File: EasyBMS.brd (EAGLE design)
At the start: 49 x 100 mm, 166 parts, among them IC1 LM2596S-5.0_NOPB, IC2 LTC6811IG-1#PBF, Q10 BSS84LT1G, Q11 BSS84LT1G, Q12 BSS84LT1G, Q13 BSS84LT1G, Q2 BSS84LT1G, Q3 BSS84LT1G, Q4 BSS84LT1G, Q5 BSS84LT1G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

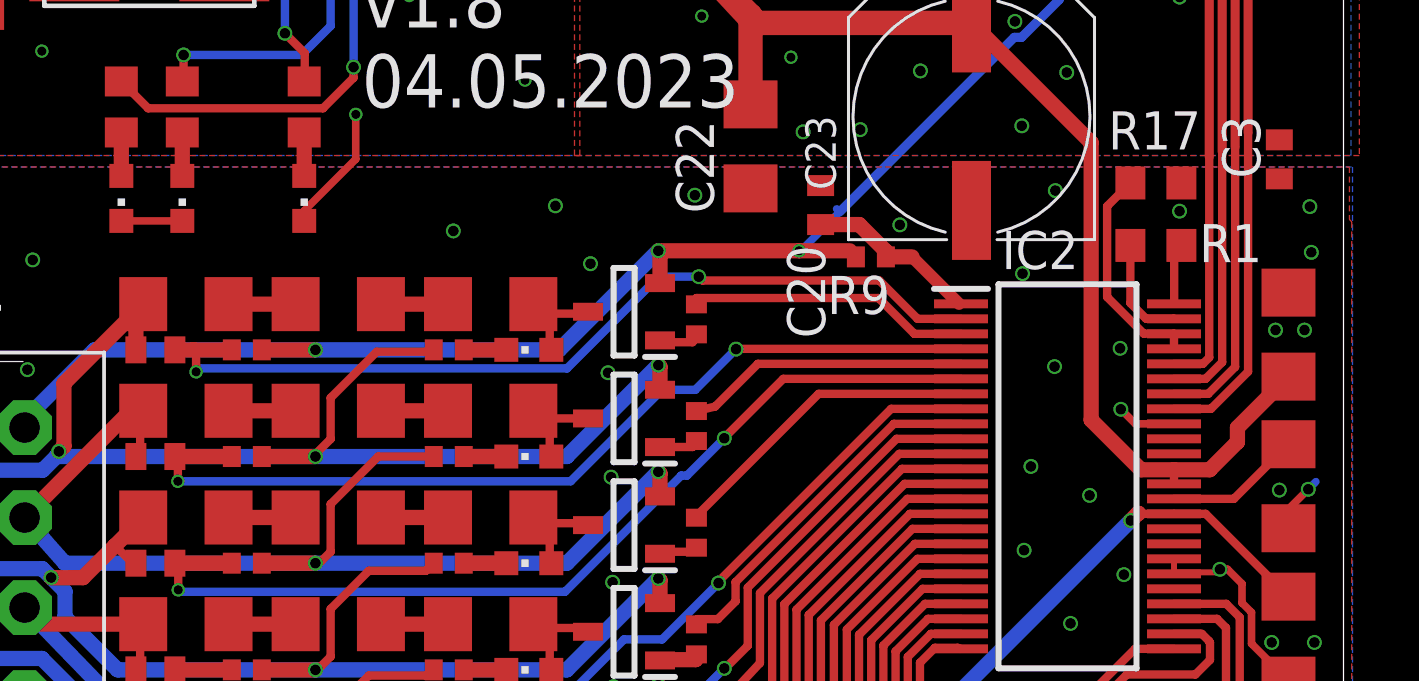
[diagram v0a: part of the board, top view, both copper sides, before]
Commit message: bug on 2 LEDs removed, new production files generated
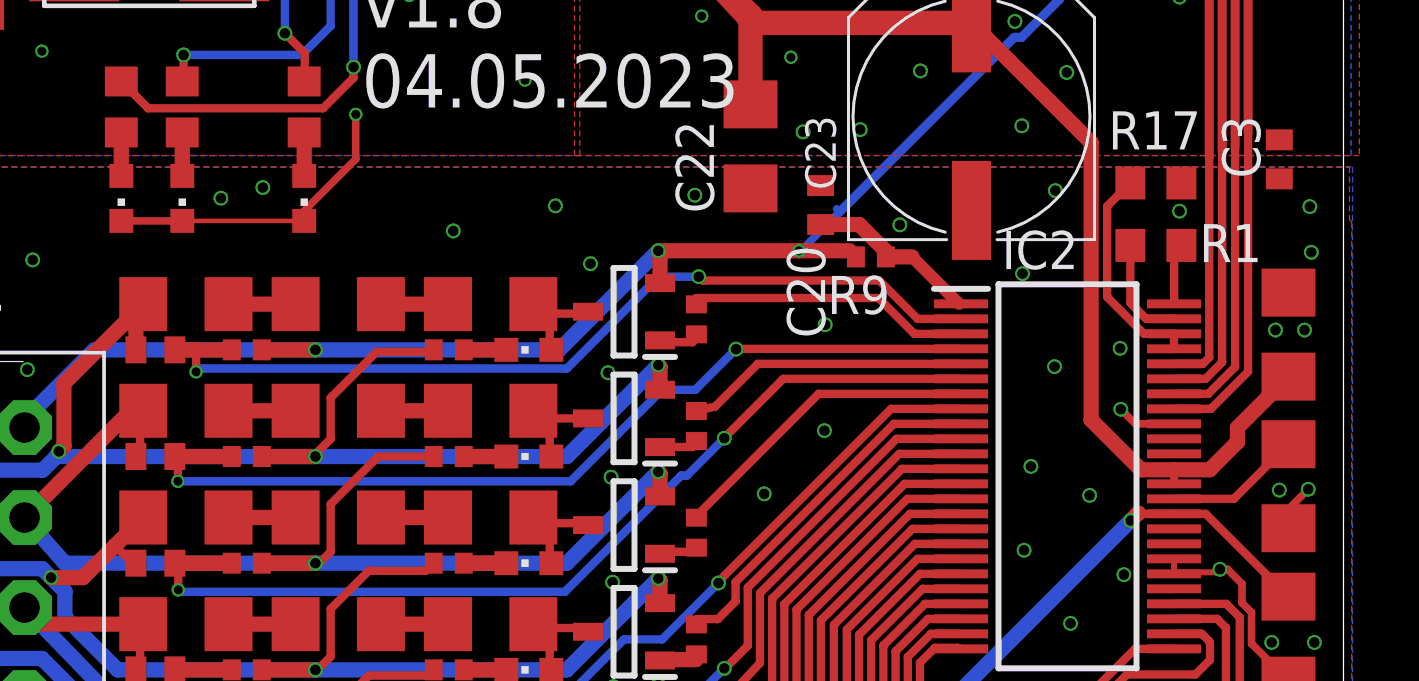
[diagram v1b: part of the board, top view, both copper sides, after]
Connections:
- removed net N$3: LED1.C, LED2.C
- net GND: now also LED1.C, LED2.C
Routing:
- net GND: track 40.3 -> 46.4 mm
- net N$3: track 2.03 -> 0.00 mm
- net GND2: track 10.9 -> 10.5 mm, vias 70 -> 75
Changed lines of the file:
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@@
 <via x="44.958" y="79.74" extent="1-16" drill="0.3"/>
 <via x="44.8056" y="76.6158" extent="1-16" drill="0.3"/>
+<contactref element="LED2" pad="C"/>
+<contactref element="LED1" pad="C"/>
+<wire x1="10.2944" y1="50.2718" x2="8.2624" y2="50.2718" width="0.254" layer="1"/>
+<wire x1="10.2944" y1="50.2718" x2="14.3584" y2="50.2718" width="0.1524" layer="1"/>
 </signal>
 <signal name="N$202">
@@
 <wire x1="47.1678" y1="40.6654" x2="47.8282" y2="41.3258" width="0.254" layer="1"/>
 <via x="47.8282" y="41.3258" extent="1-16" drill="0.35"/>
-<wire x1="47.8282" y1="41.3258" x2="48.0822" y2="41.5798" width="0.254" layer="16"/>
 <via x="47.7012" y="46.6344" extent="1-16" drill="0.35"/>
 <via x="46.863" y="41.3004" extent="1-16" drill="0.35"/>
@@
 <via x="38.3032" y="48.514" extent="1-16" drill="0.35"/>
 <via x="38.5826" y="42.0878" extent="1-16" drill="0.35"/>
-</signal>
-<signal name="N$3">
-<contactref element="LED2" pad="C"/>
-<contactref element="LED1" pad="C"/>
-<wire x1="10.2944" y1="50.2718" x2="8.2624" y2="50.2718" width="0.254" layer="1"/>
+<via x="12.9794" y="51.3842" extent="1-16" drill="0.35"/>
+<via x="11.5824" y="51.0286" extent="1-16" drill="0.35"/>
+<via x="31.6992" y="43.2816" extent="1-16" drill="0.35"/>
+<via x="29.6926" y="41.1734" extent="1-16" drill="0.35"/>
+<via x="31.7246" y="46.8122" extent="1-16" drill="0.35"/>
 </signal>
 <signal name="A0DC">

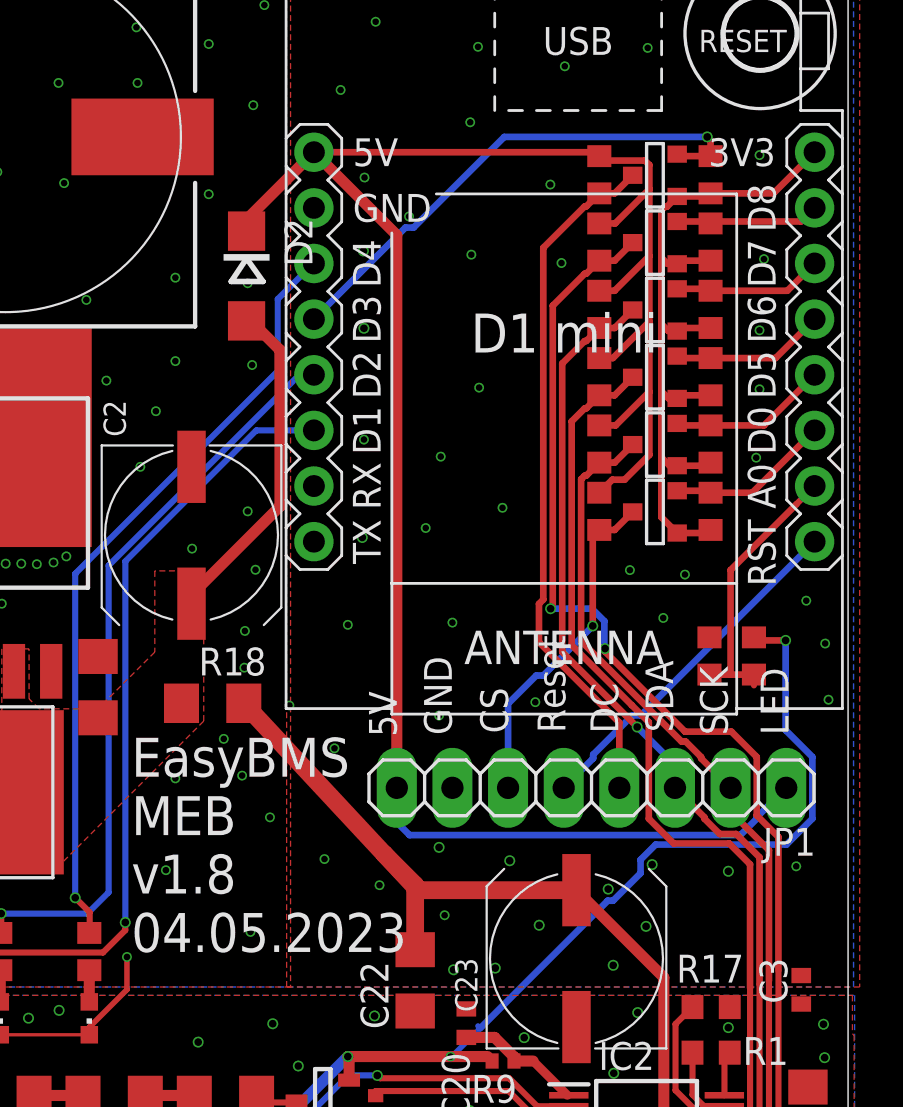
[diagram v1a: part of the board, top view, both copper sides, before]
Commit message: level shifter removed
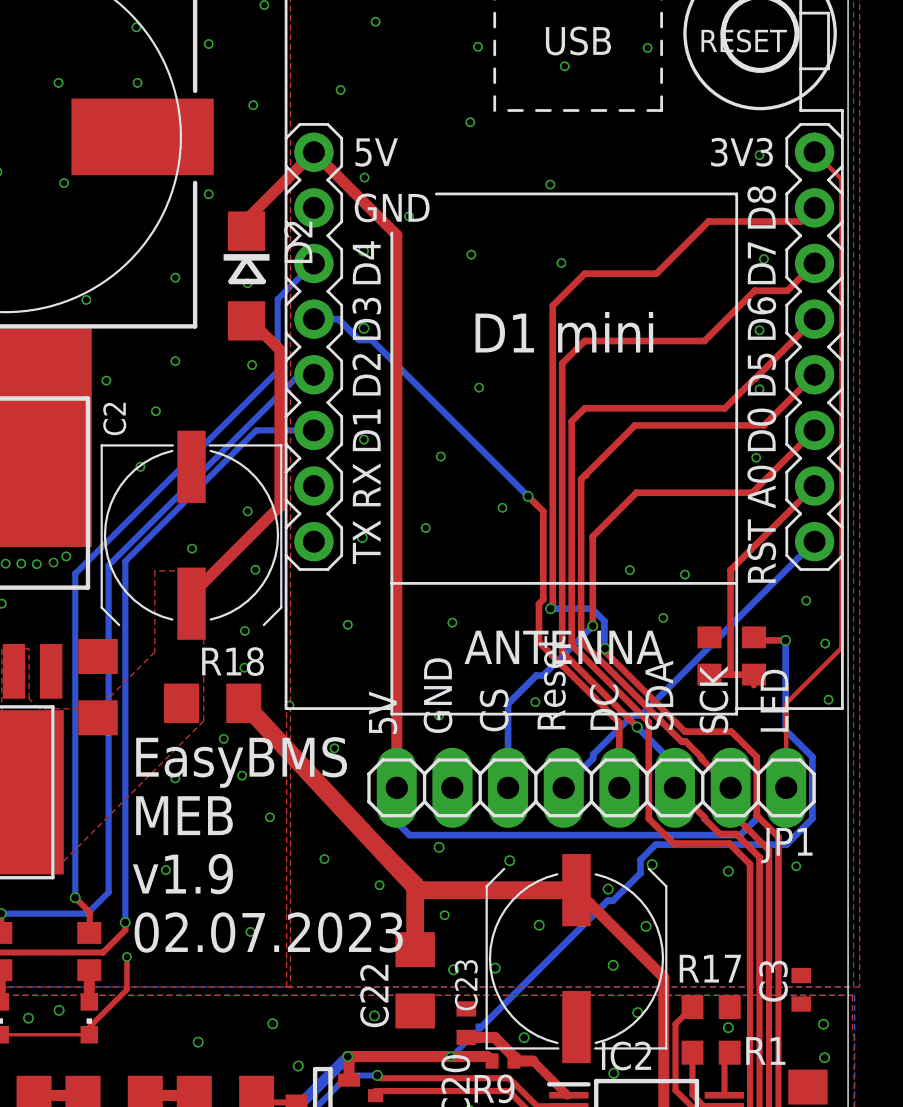
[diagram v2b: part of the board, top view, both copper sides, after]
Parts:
- removed R100, R101, R102, R103, R55, R59, R60, R82, R96, R97, R98, R99: 10k, rcl:R0603
- removed T1, T2, T3, T4, T5, T6: C8545, zetex:SOT-23
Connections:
- removed net A0DC: JP1.4, R101.1, T5.1
- removed net CSB: IC2.41, R99.1, T4.1
- removed net CSDSPLESP: R102.1, T6.2, U$2.JP1.3
- removed net CSLTCESP: R98.1, T4.2, U$2.JP1.7
- removed net MISOESP: R60.1, T2.2, U$2.JP1.5
- removed net MOSIESP: R96.1, T3.2, U$2.JP1.6
- removed net SCKESP: R55.1, T1.2, U$2.JP1.4
- new net CSLTC: IC2.41, U$2.JP1.7
- net +3V3: now also JP1.1; no longer R100.2, R102.2, R55.2, R60.2, R96.2, R98.2, T1.3, T2.3, T3.3, T4.3, T5.3, T6.3
- net 5VINESP: no longer JP1.1, R101.2, R103.2, R59.2, R82.2, R97.2, R99.2
- net CSDSPL: now also U$2.JP1.3; no longer R103.1, T6.1
- net D3: now also JP1.4; no longer R100.1, T5.2
- net MISO: now also U$2.JP1.5; no longer R82.1, T2.1
- net MOSI: now also U$2.JP1.6; no longer R97.1, T3.1
- net SCK: now also U$2.JP1.4; no longer R59.1, T1.1
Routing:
- net CSLTC: track 0.00 -> 61.8 mm, vias 0 -> 2
- net CSB: track 52.8 -> 0.00 mm, vias 2 -> 0
- net 5VINESP: track 99.6 -> 54.1 mm
- net A0DC: track 31.7 -> 0.00 mm
- net CSDSPL: track 15.5 -> 25.4 mm
- net SCK: track 39.3 -> 49.0 mm
- net MISO: track 42.3 -> 51.7 mm
- net MOSI: track 45.6 -> 54.8 mm
- net CSDSPLESP: track 7.49 -> 0.00 mm
- net SCKESP: track 7.27 -> 0.00 mm
- net MISOESP: track 7.05 -> 0.00 mm
- net MOSIESP: track 6.83 -> 0.00 mm
- net CSLTCESP: track 6.66 -> 0.00 mm
- net D3: track 23.9 -> 28.3 mm
- net +3V3: track 34.5 -> 30.6 mm
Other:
- board text added: "EasyBMS MEB v1.9 02.07.2023"
- board text removed: "EasyBMS MEB v1.8 04.05.2023"

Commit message: design blocks added
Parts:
- added R2: 10k, rcl:R1206
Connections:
- net +3V3: now also R2.2
- net MISO: now also R2.1
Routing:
- net +3V3: track 30.6 -> 40.0 mm
- net MISO: track 51.7 -> 54.0 mm
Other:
- board text added: "EasyBMS MEB v2.0 03.08.2023"
- board text removed: "EasyBMS MEB v1.9 02.07.2023"
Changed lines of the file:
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@@
 <text x="16.2814" y="54.0512" size="1.778" layer="25">EasyBMS
 MEB
-v1.9
-02.07.2023</text>
+v2.0
+03.08.2023</text>
 <text x="30.9118" y="63.9572" size="1.27" layer="25" rot="R90">GND</text>
 <text x="28.3972" y="63.881" size="1.27" layer="25" rot="R90">5V</text>
@@
 <attribute name="VALUE" x="47.4472" y="64.7192" size="1.27" layer="27" rot="R180"/>
 </element>
+<element name="R2" library="rcl" library_urn="urn:adsk.eagle:library:334" package="R1206" package3d_urn="urn:adsk.eagle:package:23540/2" value="10k" x="40.3606" y="80.4672" smashed="yes">
+<attribute name="NAME" x="39.0906" y="81.7372" size="1.27" layer="25"/>
+<attribute name="POPULARITY" value="41" x="40.3606" y="80.4672" size="1.778" layer="27" display="off"/>
+<attribute name="SPICEPREFIX" value="R" x="40.3606" y="80.4672" size="1.778" layer="27" display="off"/>
+<attribute name="VALUE" x="39.0906" y="77.9272" size="1.27" layer="27"/>
+</element>
 </elements>
 <signals>
@@
 <wire x1="44.74856875" y1="80.2456" x2="43.37376875" y2="78.8708" width="0.3048" layer="1"/>
 <wire x1="47.4726" y1="82.9432" x2="44.775" y2="80.2456" width="0.3048" layer="1"/>
-<wire x1="43.37376875" y1="78.8708" x2="36.97706875" y2="78.8708" width="0.3048" layer="1"/>
+<wire x1="43.37376875" y1="78.8708" x2="37.3422" y2="78.8708" width="0.3048" layer="1"/>
+<contactref element="R2" pad="1"/>
+<wire x1="38.9386" y1="80.4672" x2="37.3422" y2="78.8708" width="0.3048" layer="1"/>
+<wire x1="37.3422" y1="78.8708" x2="36.97706875" y2="78.8708" width="0.3048" layer="1"/>
 </signal>
 <signal name="GND">
@@
 <wire x1="46.1772" y1="65.405" x2="48.6984" y2="67.9262" width="0.2032" layer="1"/>
 <wire x1="48.6984" y1="89.3374" x2="47.4726" y2="90.5632" width="0.2032" layer="1"/>
-<wire x1="48.6984" y1="67.9262" x2="48.6984" y2="89.3374" width="0.2032" layer="1"/>
+<wire x1="48.6984" y1="67.9262" x2="48.6984" y2="85.5472" width="0.2032" layer="1"/>
+<contactref element="R2" pad="2"/>
+<wire x1="48.6984" y1="85.5472" x2="48.6984" y2="89.3374" width="0.2032" layer="1"/>
+<wire x1="48.6984" y1="85.5472" x2="48.6012" y2="85.45" width="0.2032" layer="1"/>
+<wire x1="48.6012" y1="85.45" x2="48.6012" y2="85.0157125" width="0.2032" layer="1"/>
+<wire x1="48.6012" y1="85.0157125" x2="47.6572875" y2="84.0718" width="0.2032" layer="1"/>
+<wire x1="47.6572875" y1="84.0718" x2="47.0051125" y2="84.0718" width="0.2032" layer="1"/>
+<wire x1="47.0051125" y1="84.0718" x2="45.4128" y2="82.4794875" width="0.2032" layer="1"/>
+<wire x1="45.4128" y1="82.4794875" x2="45.4128" y2="82.2440125" width="0.2032" layer="1"/>
+<wire x1="45.4128" y1="82.2440125" x2="43.6359875" y2="80.4672" width="0.2032" layer="1"/>
+<wire x1="43.6359875" y1="80.4672" x2="41.7826" y2="80.4672" width="0.2032" layer="1"/>
 </signal>
 <signal name="IPB">

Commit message: New controller added as part
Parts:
- added IC3: ESP32-S3-WROOM-1-N4R2, SamacSys_Parts:ESP32S3WROOM1N4R2
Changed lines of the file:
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@@
 <layer number="25" name="tNames" color="7" fill="1" visible="yes" active="yes"/>
 <layer number="26" name="bNames" color="7" fill="1" visible="yes" active="yes"/>
-<layer number="27" name="tValues" color="7" fill="1" visible="no" active="yes"/>
+<layer number="27" name="tValues" color="7" fill="1" visible="yes" active="yes"/>
 <layer number="28" name="bValues" color="7" fill="1" visible="no" active="yes"/>
 <layer number="29" name="tStop" color="7" fill="3" visible="no" active="yes"/>
@@
 <attribute name="VALUE" x="39.0906" y="77.9272" size="1.27" layer="27"/>
 </element>
+<element name="IC3" library="SamacSys_Parts" package="ESP32S3WROOM1N4R2" value="ESP32-S3-WROOM-1-N4R2" x="-11.1506" y="13.6144" smashed="yes">
+<attribute name="DESCRIPTION" value="Bluetooth, WiFi 802.11b/g/n, Bluetooth v5.0 Transceiver Module 2.4GHz PCB Trace Surface Mount" x="-11.1506" y="13.6144" size="1.778" layer="27" display="off"/>
+<attribute name="HEIGHT" value="3.25mm" x="-11.1506" y="13.6144" size="1.778" layer="27" display="off"/>
+<attribute name="LCSC" value="C2913203" x="-11.1506" y="13.6144" size="1.778" layer="27"/>
+<attribute name="MANUFACTURER_NAME" value="Espressif Systems" x="-11.1506" y="13.6144" size="1.778" layer="27" display="off"/>
+<attribute name="MANUFACTURER_PART_NUMBER" value="ESP32-S3-WROOM-1-N4R2" x="-11.1506" y="13.6144" size="1.778" layer="27" display="off"/>
+<attribute name="MOUSER_PART_NUMBER" value="356-ESP32S3WROM1N4R2" x="-11.1506" y="13.6144" size="1.778" layer="27" display="off"/>
+<attribute name="MOUSER_PRICE-STOCK" value="https://www.mouser.co.uk/ProductDetail/Espressif-Systems/ESP32-S3-WROOM-1-N4R2?qs=Li%252BoUPsLEns3eX9krmrDyw%3D%3D" x="-11.1506" y="13.6144" size="1.778" layer="27" display="off"/>
+<attribute name="NAME" x="-11.3284" y="19.05" size="1.27" layer="25" align="center"/>
+<attribute name="VALUE" x="-11.1506" y="13.6144" size="1.27" layer="27" align="center"/>
+</element>
 </elements>

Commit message: dummy IC added
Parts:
- added IC4: DRV103H, SamacSys_Parts:SOIC127P600X170-9N
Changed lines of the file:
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@@
 <attribute name="VALUE" x="-11.1506" y="13.6144" size="1.27" layer="27" align="center"/>
+</element>
+<element name="IC4" library="SamacSys_Parts" package="SOIC127P600X170-9N" value="DRV103H" x="-19.3802" y="-3.2512" smashed="yes">
+<attribute name="DESCRIPTION" value="PWM Low-Side Driver 3A for Coils HSOP8 DRV103H, MOSFET Power Driver, 1.5A, Non-Inverting, 8 ??? 32 V, 8-Pin SO PowerPAD" x="-19.3802" y="-3.2512" size="1.778" layer="27" display="off"/>
+<attribute name="HEIGHT" value="1.7mm" x="-19.3802" y="-3.2512" size="1.778" layer="27" display="off"/>
+<attribute name="MANUFACTURER_NAME" value="Texas Instruments" x="-19.3802" y="-3.2512" size="1.778" layer="27" display="off"/>
+<attribute name="MANUFACTURER_PART_NUMBER" value="DRV103H" x="-19.3802" y="-3.2512" size="1.778" layer="27" display="off"/>
+<attribute name="MOUSER_PART_NUMBER" value="595-DRV103H" x="-19.3802" y="-3.2512" size="1.778" layer="27" display="off"/>
+<attribute name="MOUSER_PRICE-STOCK" value="https://www.mouser.co.uk/ProductDetail/Texas-Instruments/DRV103H/?qs=VBduBm9rCJQEx63T3F6Ttg%3D%3D" x="-19.3802" y="-3.2512" size="1.778" layer="27" display="off"/>
+<attribute name="NAME" x="-19.3802" y="-3.2512" size="1.27" layer="25" align="center"/>
+<attribute name="VALUE" x="-19.3802" y="-3.2512" size="1.27" layer="27" align="center"/>
 </element>
 </elements>
